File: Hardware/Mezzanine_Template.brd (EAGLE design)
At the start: 30.5 x 44.5 mm, 12 parts, among them U2 EDISON_CONNECTOR_FULLMOUNTING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, U3 EDISON_CONNECTOR_FULLHEADER

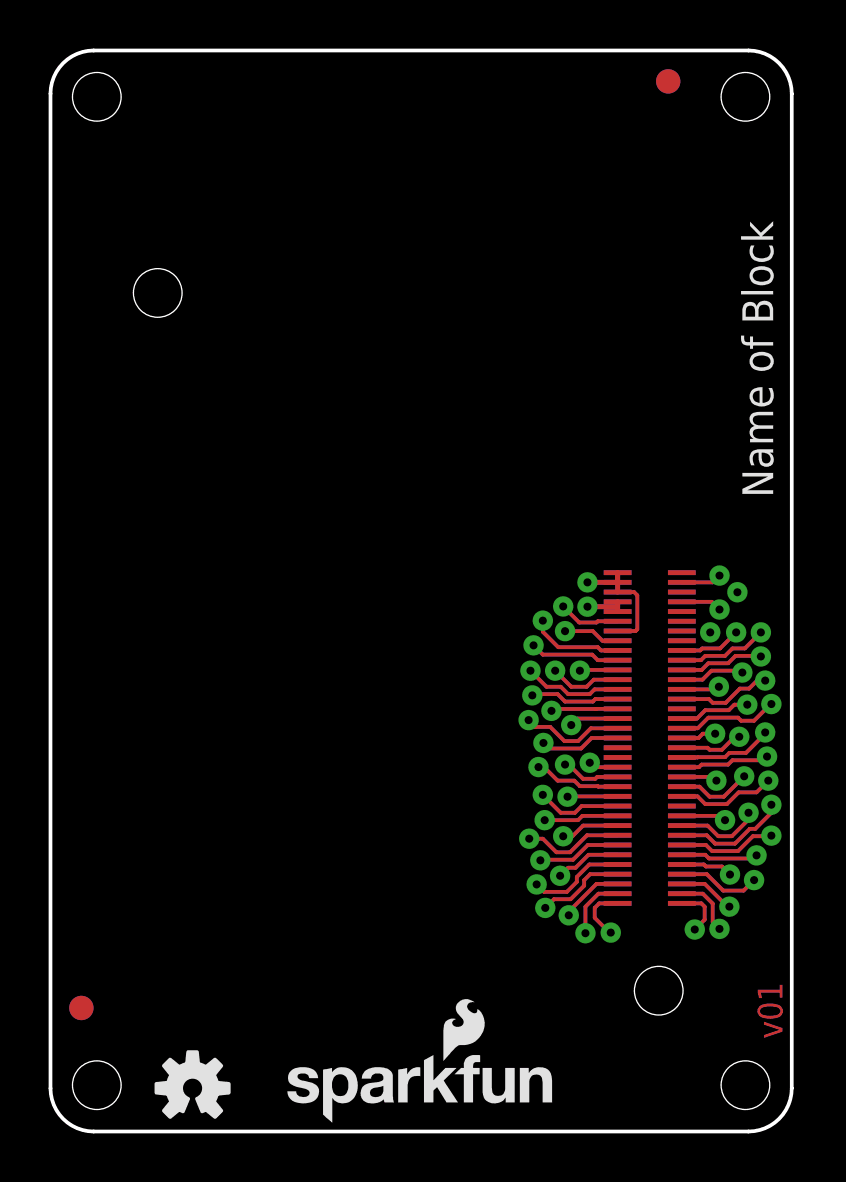
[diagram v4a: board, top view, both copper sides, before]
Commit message: clean-up
Board
- Removed duplicate CC frame
- Adjusted sizes, ratios of text so they can be read when "Always Vector
Font" is set
- Adjusted positioning and alignment of text for consistency throughout
the drawing and making the text easier to edit (expansion)
- Fixed corner radius (indicated 0.08", should be 0.07")
- Added unit to the drill hole Dimension as it is -not- in inches
- Fixed top GND plane's bottom right corner (was off a smidgen)
- Centered the SparkFun logos (wiggle wiggle)
- Adjusted version number to 'v01.x' (not for release).  Please make
sure to adjust to appropriate version number before release!

Schematic
- Changed position, ratio and alignment of 'Engineer' in the frame to
align with the rest of the text and be consistent with the board
- Adjusted version number to 'v01.x' (not for release).  Please make
sure to adjust to appropriate version number before release!
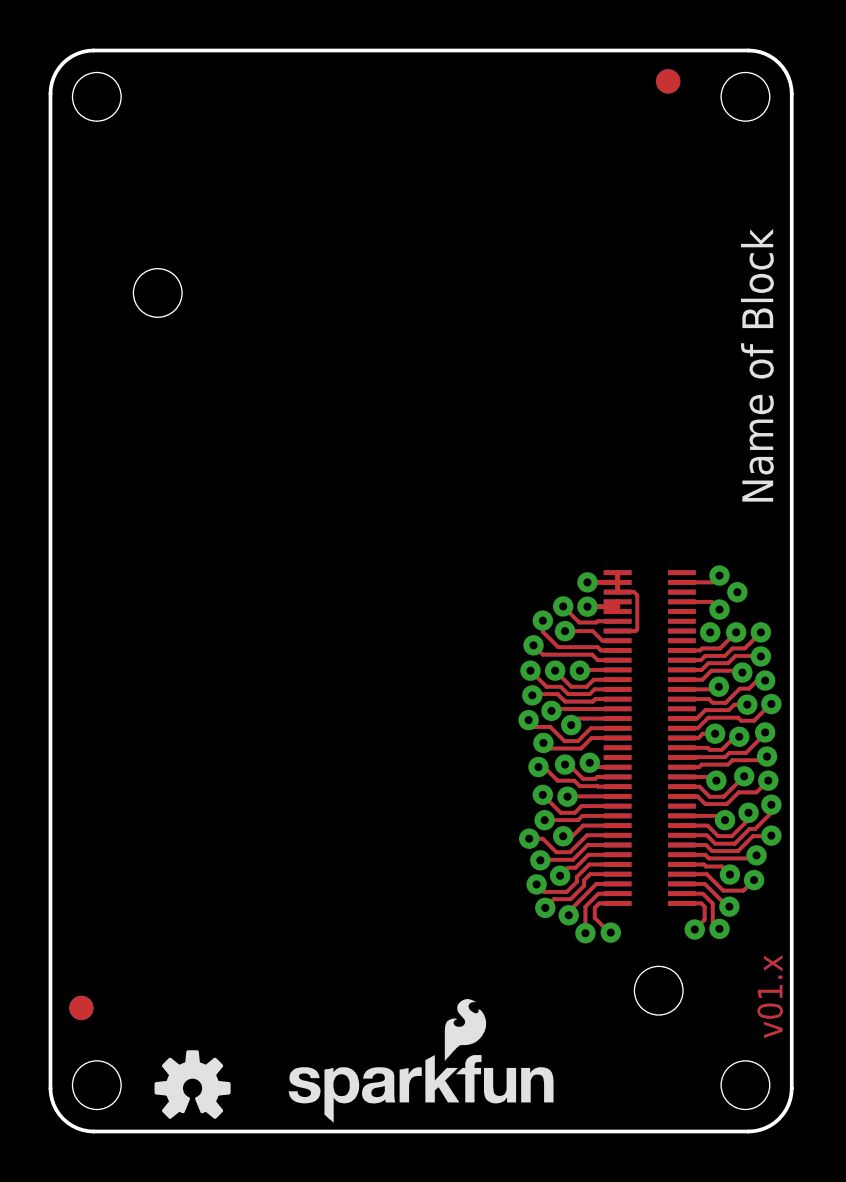
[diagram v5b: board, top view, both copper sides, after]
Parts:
- removed FRAME2: FRAME-LETTER, SparkFun-Aesthetics:CREATIVE_COMMONS
- moved LOGO4 0.06 mm to (9.35, 0.25)
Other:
- board text added: "LEDs & User Switches/Buttons go here"
- board text added: "User Interface/Connectors"
- board text added: "v01.x"
- board text removed: "LED's & User Switches/Buttons Go Here"
- board text removed: "User Interface/ Connectors"
- board text removed: "v01"
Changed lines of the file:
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@@
 <?xml version="1.0" encoding="utf-8"?>
 <!DOCTYPE eagle SYSTEM "eagle.dtd">
-<eagle version="6.6.0">
+<eagle version="6.5.0">
 <drawing>
 <settings>
@@
 <setting verticaltext="up"/>
 </settings>
-<grid distance="0.001" unitdist="inch" unit="inch" style="lines" multiple="1" display="yes" altdistance="0.005" altunitdist="inch" altunit="inch"/>
+<grid distance="0.05" unitdist="inch" unit="inch" style="lines" multiple="1" display="yes" altdistance="0.005" altunitdist="inch" altunit="inch"/>
 <layers>
 <layer number="1" name="Top" color="4" fill="1" visible="yes" active="yes"/>
@@
 <wire x1="28.702" y1="0" x2="1.778" y2="0" width="0.1524" layer="20"/>
 <wire x1="0" y1="1.778" x2="0" y2="42.672" width="0.1524" layer="20"/>
-<text x="25.4" y="-13.97" size="1.6764" layer="51" ratio="15">Engineer</text>
+<text x="29.21" y="-13.97" size="1.6764" layer="51" ratio="15">Engineer</text>
 <hole x="28.575" y="1.905" drill="2"/>
 <hole x="1.905" y="1.905" drill="2"/>
 <hole x="1.905" y="42.545" drill="2"/>
 <hole x="28.575" y="42.545" drill="2"/>
-<text x="8.255" y="45.085" size="1.778" layer="51">User Interface/
- Connectors</text>
-<text x="-2.54" y="41.91" size="1.778" layer="51" rot="R270">LED's &amp; User Switches/Buttons Go Here</text>
-<text x="31.115" y="39.37" size="1.778" layer="51" rot="R270">Nothing goes here...  I mean it.</text>
-<text x="29.083" y="31.75" size="1.27" layer="21" font="vector" ratio="15" rot="R90" align="center">Name of Block</text>
+<text x="15.24" y="45.085" size="1.27" layer="51" align="bottom-center">User Interface/Connectors</text>
+<text x="-0.635" y="22.225" size="1.27" layer="51" rot="R270" align="top-center">LEDs &amp; User Switches/Buttons go here</text>
+<text x="31.115" y="22.225" size="1.27" layer="51" rot="R270" align="bottom-center">Nothing goes here...  I mean it.</text>
+<text x="29.718" y="25.74798125" size="1.27" layer="21" font="vector" ratio="15" rot="R90">Name of Block</text>
 <wire x1="1.778" y1="44.45" x2="28.702" y2="44.45" width="0.1524" layer="20"/>
-<wire x1="30.48" y1="44.704" x2="30.48" y2="53.34" width="0.254" layer="51"/>
+<wire x1="30.48" y1="46.99" x2="30.48" y2="53.34" width="0.254" layer="51"/>
 <wire x1="30.48" y1="53.34" x2="0" y2="53.34" width="0.254" layer="51"/>
-<wire x1="0" y1="53.34" x2="0" y2="44.704" width="0.254" layer="51"/>
+<wire x1="0" y1="53.34" x2="0" y2="46.99" width="0.254" layer="51"/>
 <wire x1="30.48" y1="1.778" x2="28.702" y2="0" width="0.1524" layer="20" curve="-90"/>
 <wire x1="1.778" y1="0" x2="0" y2="1.778" width="0.1524" layer="20" curve="-90"/>
 <wire x1="0" y1="42.672" x2="1.778" y2="44.45" width="0.1524" layer="20" curve="-90"/>
 <wire x1="28.702" y1="44.45" x2="30.48" y2="42.672" width="0.1524" layer="20" curve="-90"/>
-<text x="14.986" y="54.356" size="1.27" layer="51" ratio="15" align="center">Max Board Length</text>
-<dimension x1="28.575" y1="1.905" x2="1.905" y2="1.905" x3="15.24" y3="-2.54" textsize="1.27" textratio="15" layer="51" dtype="horizontal" unit="inch"/>
-<dimension x1="30.48" y1="1.728" x2="0" y2="2.54" x3="15.24" y3="-5.08" textsize="1.27" textratio="15" layer="51" dtype="horizontal" unit="inch"/>
-<dimension x1="1.905" y1="42.545" x2="1.905" y2="1.905" x3="35.56" y3="22.225" textsize="1.27" textratio="15" layer="51" dtype="vertical" unit="inch"/>
-<dimension x1="1.778" y1="44.45" x2="5.08" y2="0" x3="38.1" y3="22.225" textsize="1.27" textratio="15" layer="51" dtype="vertical" unit="inch"/>
-<dimension x1="0" y1="53.34" x2="2.54" y2="0" x3="40.64" y3="26.67" textsize="1.27" textratio="15" layer="51" dtype="vertical" unit="inch"/>
+<text x="15.24" y="53.975" size="1.27" layer="51" align="bottom-center">Max Board Length</text>
+<dimension x1="28.575" y1="1.905" x2="1.905" y2="1.905" x3="15.24" y3="-2.54" textsize="1.27" textratio="10" layer="51" dtype="horizontal" unit="inch"/>
+<dimension x1="30.48" y1="1.728" x2="0" y2="2.54" x3="15.24" y3="-5.08" textsize="1.27" textratio="10" layer="51" dtype="horizontal" unit="inch"/>
+<dimension x1="1.905" y1="42.545" x2="1.905" y2="1.905" x3="35.56" y3="22.225" textsize="1.27" textratio="10" layer="51" dtype="vertical" unit="inch"/>
+<dimension x1="1.778" y1="44.45" x2="5.08" y2="0" x3="38.1" y3="22.225" textsize="1.27" textratio="10" layer="51" dtype="vertical" unit="inch"/>
+<dimension x1="0" y1="53.34" x2="2.54" y2="0" x3="40.64" y3="26.67" textsize="1.27" textratio="10" layer="51" dtype="vertical" unit="inch"/>
 <rectangle x1="22.098" y1="26.162" x2="30.48" y2="44.45" layer="42" rot="R180"/>
 <rectangle x1="22.098" y1="26.162" x2="30.48" y2="44.45" layer="41" rot="R180"/>
-<dimension x1="1.905" y1="42.545" x2="0.4190875" y2="43.81858125" x3="-5.503225" y3="48.894621875" textsize="1.778" layer="51" dtype="radius" unit="inch"/>
-<dimension x1="29.28210625" y1="41.83789375" x2="27.86789375" y2="43.25210625" x3="34.29" y3="48.26" textsize="1.778" layer="51" dtype="diameter"/>
+<dimension x1="1.905" y1="42.545" x2="0.5579625" y2="43.8920375" x3="-5.07986875" y3="49.285071875" textsize="1.27" textratio="10" layer="51" dtype="radius" unit="inch"/>
+<dimension x1="29.28210625" y1="41.83789375" x2="27.86789375" y2="43.25210625" x3="34.925" y3="48.895" textsize="1.27" textratio="10" layer="51" dtype="diameter" visible="yes"/>
+<text x="30.099" y="3.81" size="1.016" layer="1" font="vector" ratio="15" rot="R90">v01.x</text>
+<text x="33.02" y="-3.81" size="1.778" layer="51">Note: Units are in Inches</text>
+<text x="29.718" y="40.005" size="1.27" layer="22" font="vector" ratio="15" rot="SMR270">Name of Block</text>
 <text x="29.21" y="6.35" size="1.016" layer="22" font="vector" ratio="15" rot="MR90" align="center">4xM2.0</text>
-<text x="30.099" y="3.81" size="1.016" layer="1" font="vector" ratio="15" rot="R90">v01</text>
-<text x="33.02" y="-3.81" size="1.778" layer="51">Note: Units are in Inches</text>
-<text x="29.083" y="31.75" size="1.27" layer="22" font="vector" ratio="15" rot="SMR270" align="center">Name of Block</text>
 </plain>
 <attributes>
@@
 <element name="FRAME1" library="SparkFun-Aesthetics" package="CREATIVE_COMMONS" value="FRAME-LETTER" x="-1.27" y="-13.97"/>
 <element name="LOGO2" library="SparkFun-Aesthetics" package="OSHW-LOGO-S" value="OSHW-LOGOS" x="5.842" y="1.778" rot="MR0"/>
-<element name="LOGO3" library="SparkFun-Aesthetics" package="SFE_LOGO_NAME_FLAME_.1" value="SFE_LOGO_NAME_FLAME.1_INCH" x="21.082" y="0.254" rot="MR0"/>
+<element name="LOGO3" library="SparkFun-Aesthetics" package="SFE_LOGO_NAME_FLAME_.1" value="SFE_LOGO_NAME_FLAME.1_INCH" x="21.125003125" y="0.254" rot="MR0"/>
 <element name="U2" library="Edison" package="EDISON_DAUGHTER" value="EDISON_CONNECTOR_FULLMOUNTING_HOLES" x="27.94" y="3.81" rot="MR0"/>
 <element name="U3" library="Edison" package="DF40C-70DP-0.4(51)" value="EDISON_CONNECTOR_FULLHEADER" x="24.64" y="16.1798" rot="MR90"/>
-<element name="FRAME2" library="SparkFun-Aesthetics" package="CREATIVE_COMMONS" value="FRAME-LETTER" x="-1.27" y="-13.97"/>
 <element name="LOGO1" library="SparkFun-Aesthetics" package="OSHW-LOGO-S" value="OSHW-LOGOS" x="5.842" y="1.778"/>
-<element name="LOGO4" library="SparkFun-Aesthetics" package="SFE_LOGO_NAME_FLAME_.1" value="SFE_LOGO_NAME_FLAME.1_INCH" x="9.2964" y="0.254"/>
+<element name="LOGO4" library="SparkFun-Aesthetics" package="SFE_LOGO_NAME_FLAME_.1" value="SFE_LOGO_NAME_FLAME.1_INCH" x="9.354996875" y="0.254"/>
 <element name="FID1" library="SparkFun-Aesthetics" package="FIDUCIAL-1X2" value="FIDUCIAL1X2" x="1.27" y="5.08"/>
 <element name="FID2" library="SparkFun-Aesthetics" package="FIDUCIAL-1X2" value="FIDUCIAL1X2" x="25.4" y="43.18"/>
@@
 </polygon>
 <polygon width="0.1778" layer="1" spacing="0.254" rank="6">
-<vertex x="30.48" y="1.728" curve="-90"/>
+<vertex x="30.48" y="1.778" curve="-90"/>
 <vertex x="28.752" y="0"/>
 <vertex x="1.778" y="0" curve="-90"/>
@@
 </board>
 </drawing>
-<compatibility>
-<note version="6.3" minversion="6.2.2" severity="warning">
-Since Version 6.2.2 text objects can contain more than one line,
-which will not be processed correctly with this version.
-</note>
-</compatibility>
 </eagle>

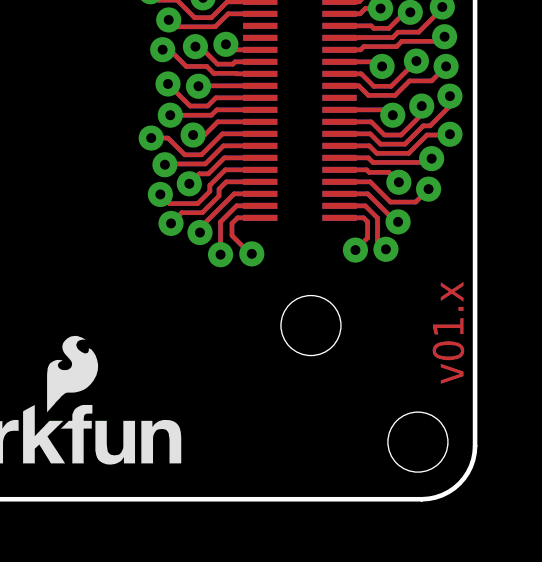
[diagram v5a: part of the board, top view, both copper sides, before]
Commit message: replaced some changes made in pull request. updated git ignore to remover .epf
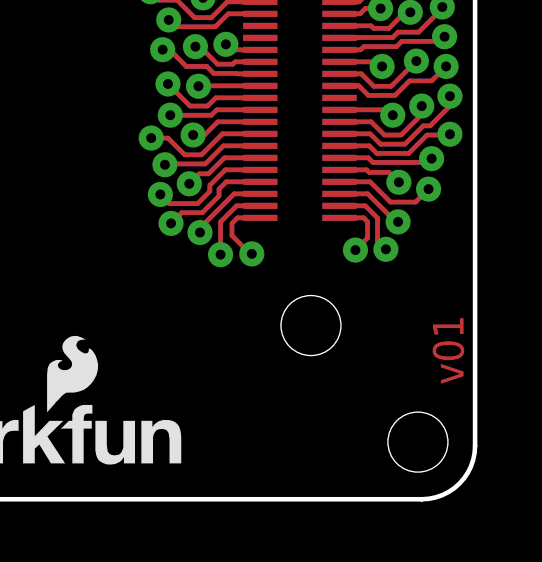
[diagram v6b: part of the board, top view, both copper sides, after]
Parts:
- added FRAME2: FRAME-LETTER, SparkFun-Aesthetics:CREATIVE_COMMONS
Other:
- board text added: "v01"
- board text removed: "v01.x"
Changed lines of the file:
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@@
 <dimension x1="1.905" y1="42.545" x2="0.5579625" y2="43.8920375" x3="-5.07986875" y3="49.285071875" textsize="1.27" textratio="10" layer="51" dtype="radius" unit="inch"/>
 <dimension x1="29.28210625" y1="41.83789375" x2="27.86789375" y2="43.25210625" x3="34.925" y3="48.895" textsize="1.27" textratio="10" layer="51" dtype="diameter" visible="yes"/>
-<text x="30.099" y="3.81" size="1.016" layer="1" font="vector" ratio="15" rot="R90">v01.x</text>
+<text x="30.099" y="3.81" size="1.016" layer="1" font="vector" ratio="15" rot="R90">v01</text>
 <text x="33.02" y="-3.81" size="1.778" layer="51">Note: Units are in Inches</text>
 <text x="29.718" y="40.005" size="1.27" layer="22" font="vector" ratio="15" rot="SMR270">Name of Block</text>
@@
 <element name="FID3" library="SparkFun-Aesthetics" package="FIDUCIAL-1X2" value="FIDUCIAL1X2" x="1.27" y="5.08" rot="MR0"/>
 <element name="FID4" library="SparkFun-Aesthetics" package="FIDUCIAL-1X2" value="FIDUCIAL1X2" x="25.4" y="43.18" rot="MR0"/>
+<element name="FRAME2" library="SparkFun-Aesthetics" package="CREATIVE_COMMONS" value="FRAME-LETTER" x="-1.27" y="-13.97"/>
 </elements>
 <signals>

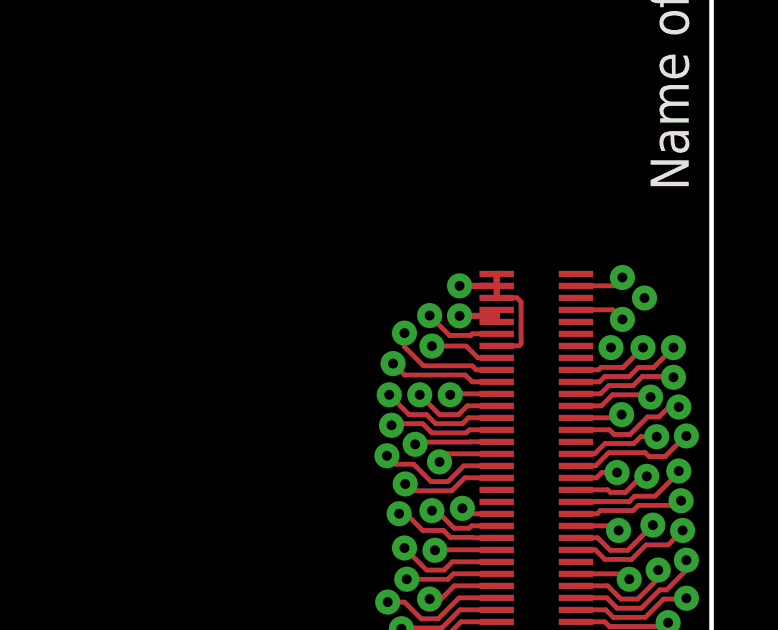
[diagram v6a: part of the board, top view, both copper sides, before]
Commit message: modified:   Hardware/Edison.lbr 	Corrected DCIN pin name on all schematic drawings
	modified:   Hardware/Mezzanine_Template.brd
	Re-positioned Vias to accomidate extra DCIN via
	Removed connection between VSYS and DCIN for boards
	that want to use battery monitoring features

	modified:   Hardware/Mezzanine_Template.sch
	Updated Schematic with current Lib Parts
	Added Note for DCIN pin usage.
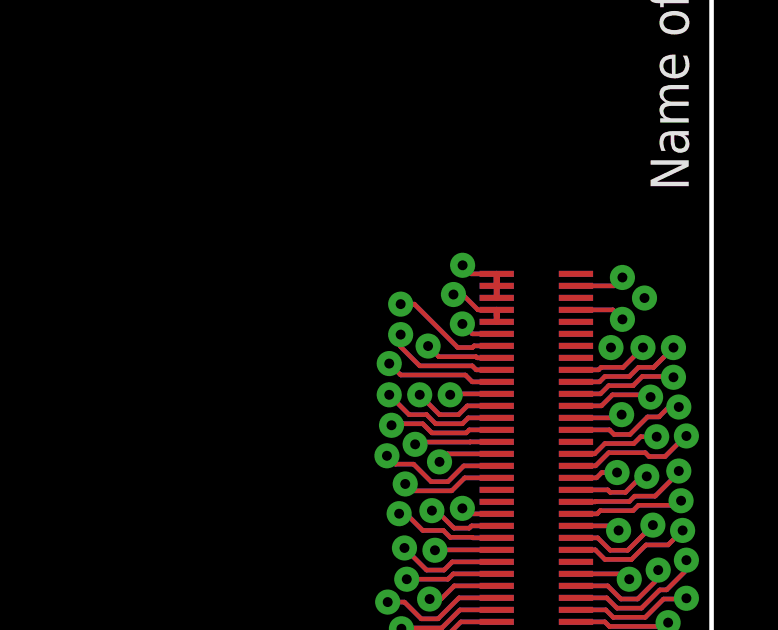
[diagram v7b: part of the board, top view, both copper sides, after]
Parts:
- removed FRAME2: FRAME-LETTER, SparkFun-Aesthetics:CREATIVE_COMMONS
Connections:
- new net DCIN: U2.14, U3.14
- net VSYS: no longer U2.14, U3.14
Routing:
- net DCIN: track 0.00 -> 7.65 mm, vias 0 -> 1
- net VSYS: track 10.7 -> 4.51 mm
- net 1.8V: track 5.07 -> 2.57 mm
- net 3.3V: track 3.68 -> 4.51 mm
